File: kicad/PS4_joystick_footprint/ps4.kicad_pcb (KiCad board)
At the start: 2 copper layers, 55.5 x 30 mm, 6 parts, among them J1 Conn_01x11_Pin, SW1 X, SW2 A, SW3 B, SW4 Y, U1 COM-09032

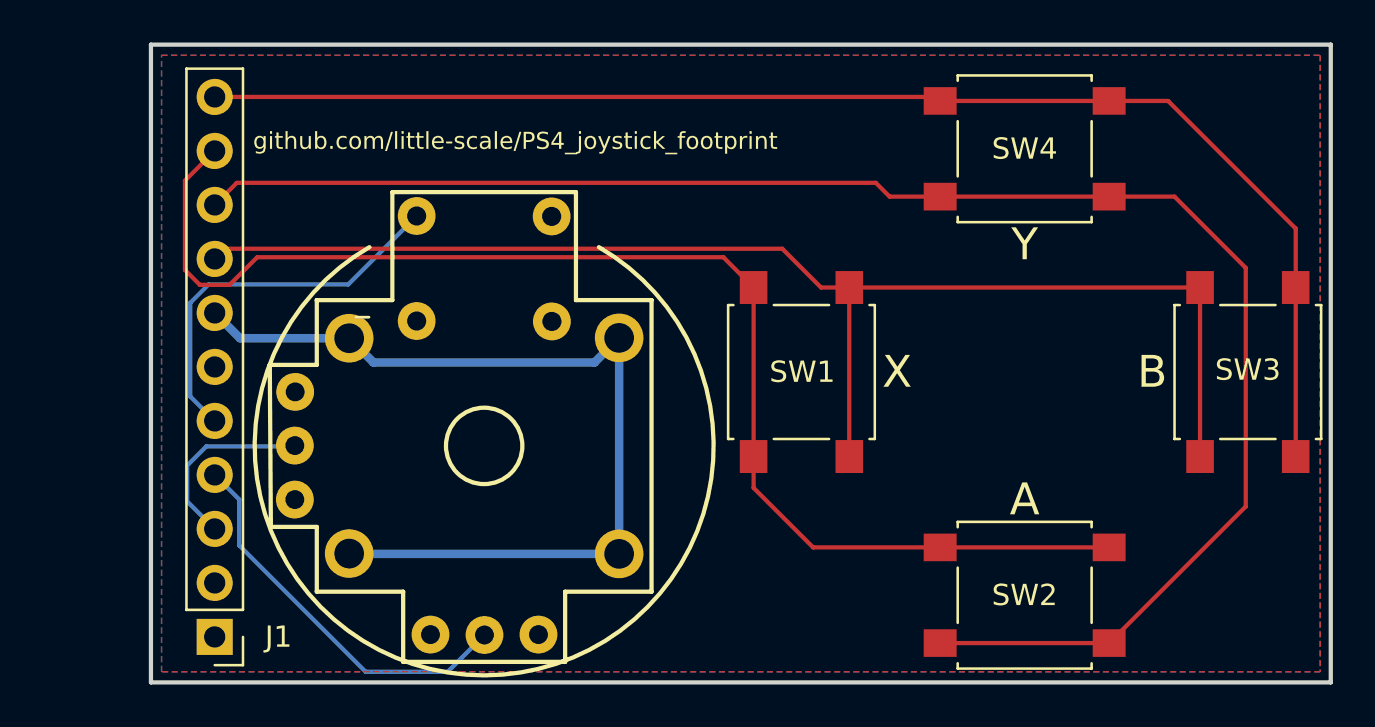
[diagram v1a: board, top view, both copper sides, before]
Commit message: optimize ps4 joystick pcb
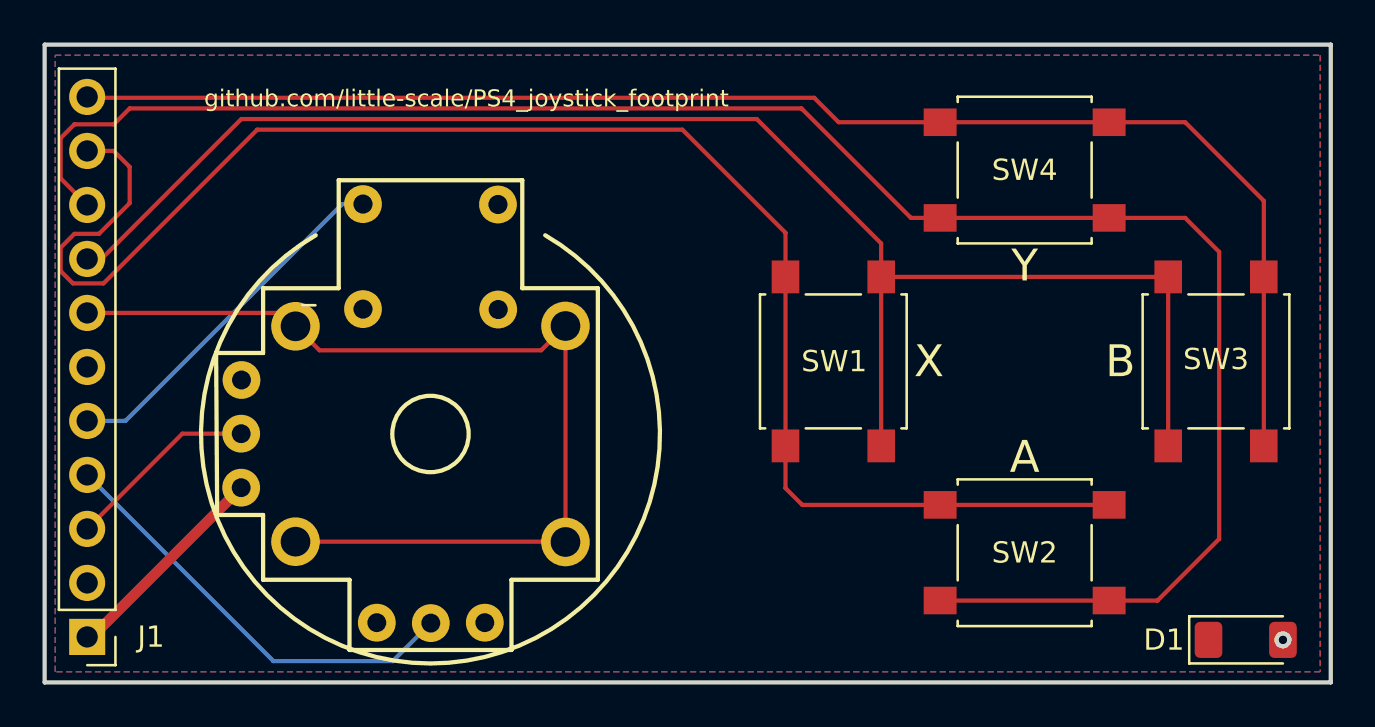
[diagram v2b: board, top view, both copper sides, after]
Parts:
- added D1: D, Diode_SMD:D_MiniMELF, F.Cu at (140.4, 153.1)
- moved J1 6.00 mm to (85.9, 153.0)
- moved U1 2.59 mm to (102.0, 143.4)
- moved SW2 2.00 mm to (130.0, 149.0)
- moved SW1 1.58 mm to (121.0, 140.0)
- moved SW3 1.58 mm to (139.0, 140.0)
- moved SW4 1.00 mm to (130.0, 131.0)
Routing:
- net /R1: track 61.7 -> 76.1 mm
- net GND: track 0.00 -> 10.7 mm, vias 0 -> 1
- net /L2: track 78.9 -> 89.4 mm
- net /L1: track 63.2 -> 73.5 mm
- net /R2: track 64.1 -> 68.9 mm
- net /Schield: track 43.3 -> 46.6 mm
- net /R_orange: track 18.5 -> 20.5 mm
- net /Switch: track 18.4 -> 17.2 mm
- added copper zone on F.Cu, net +5V
- added copper zone on B.Cu, net GND
- removed copper zone on B.Cu, net +5V
- removed copper zone on F.Cu, net GND
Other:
- board size 55.5 x 30 mm -> 60.5 x 30 mm
